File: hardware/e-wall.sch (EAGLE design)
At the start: 20 parts, among them IC1 74HCT595N, IC2 74HCT595N, IC3 74HCT595N, IC4 ULN2803, IC5 ULN2803, IC6 ULN2803, T1 BC547, T2 BC557, T3 BC547

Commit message: Spannungsteiler für SOMI
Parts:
- added R8: 20k, resistor:R-EU_0309/10
- added R9: 30k, resistor:R-EU_0309/10
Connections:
- new net N$28: R8.1, R9.2, U$1.14
- net GND: now also R9.1
- net SOMI: now also R8.2; no longer U$1.14
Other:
- note added: "Treiber"
- note removed: "Treiber für LED"
- note removed: "Treiber für Lüfter"
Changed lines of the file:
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@@
 <grid distance="0.1" unitdist="inch" unit="inch" style="lines" multiple="1" display="no" altdistance="0.01" altunitdist="inch" altunit="inch"/>
 <layers>
-<layer number="1" name="Top" color="4" fill="1" visible="yes" active="no"/>
-<layer number="16" name="Bottom" color="1" fill="1" visible="yes" active="no"/>
-<layer number="17" name="Pads" color="2" fill="1" visible="yes" active="no"/>
-<layer number="18" name="Vias" color="2" fill="1" visible="yes" active="no"/>
-<layer number="19" name="Unrouted" color="6" fill="1" visible="yes" active="no"/>
-<layer number="20" name="Dimension" color="15" fill="1" visible="yes" active="no"/>
-<layer number="21" name="tPlace" color="7" fill="1" visible="yes" active="no"/>
-<layer number="22" name="bPlace" color="7" fill="1" visible="yes" active="no"/>
-<layer number="23" name="tOrigins" color="15" fill="1" visible="yes" active="no"/>
-<layer number="24" name="bOrigins" color="15" fill="1" visible="yes" active="no"/>
-<layer number="25" name="tNames" color="7" fill="1" visible="yes" active="no"/>
-<layer number="26" name="bNames" color="7" fill="1" visible="yes" active="no"/>
-<layer number="27" name="tValues" color="7" fill="1" visible="yes" active="no"/>
-<layer number="28" name="bValues" color="7" fill="1" visible="yes" active="no"/>
+<layer number="1" name="Top" color="4" fill="1" visible="no" active="no"/>
+<layer number="16" name="Bottom" color="1" fill="1" visible="no" active="no"/>
+<layer number="17" name="Pads" color="2" fill="1" visible="no" active="no"/>
+<layer number="18" name="Vias" color="2" fill="1" visible="no" active="no"/>
+<layer number="19" name="Unrouted" color="6" fill="1" visible="no" active="no"/>
+<layer number="20" name="Dimension" color="15" fill="1" visible="no" active="no"/>
+<layer number="21" name="tPlace" color="7" fill="1" visible="no" active="no"/>
+<layer number="22" name="bPlace" color="7" fill="1" visible="no" active="no"/>
+<layer number="23" name="tOrigins" color="15" fill="1" visible="no" active="no"/>
+<layer number="24" name="bOrigins" color="15" fill="1" visible="no" active="no"/>
+<layer number="25" name="tNames" color="7" fill="1" visible="no" active="no"/>
+<layer number="26" name="bNames" color="7" fill="1" visible="no" active="no"/>
+<layer number="27" name="tValues" color="7" fill="1" visible="no" active="no"/>
+<layer number="28" name="bValues" color="7" fill="1" visible="no" active="no"/>
 <layer number="29" name="tStop" color="7" fill="3" visible="no" active="no"/>
 <layer number="30" name="bStop" color="7" fill="6" visible="no" active="no"/>
@@
 <layer number="35" name="tGlue" color="7" fill="4" visible="no" active="no"/>
 <layer number="36" name="bGlue" color="7" fill="5" visible="no" active="no"/>
-<layer number="37" name="tTest" color="7" fill="1" visible="yes" active="no"/>
-<layer number="38" name="bTest" color="7" fill="1" visible="yes" active="no"/>
+<layer number="37" name="tTest" color="7" fill="1" visible="no" active="no"/>
+<layer number="38" name="bTest" color="7" fill="1" visible="no" active="no"/>
 <layer number="39" name="tKeepout" color="4" fill="11" visible="no" active="no"/>
 <layer number="40" name="bKeepout" color="1" fill="11" visible="no" active="no"/>
@@
 <layer number="44" name="Drills" color="7" fill="1" visible="no" active="no"/>
 <layer number="45" name="Holes" color="7" fill="1" visible="no" active="no"/>
-<layer number="46" name="Milling" color="3" fill="1" visible="yes" active="no"/>
-<layer number="47" name="Measures" color="7" fill="1" visible="yes" active="no"/>
-<layer number="48" name="Document" color="7" fill="1" visible="yes" active="no"/>
-<layer number="49" name="Reference" color="7" fill="1" visible="yes" active="no"/>
-<layer number="51" name="tDocu" color="7" fill="1" visible="yes" active="no"/>
-<layer number="52" name="bDocu" color="7" fill="1" visible="yes" active="no"/>
+<layer number="46" name="Milling" color="3" fill="1" visible="no" active="no"/>
+<layer number="47" name="Measures" color="7" fill="1" visible="no" active="no"/>
+<layer number="48" name="Document" color="7" fill="1" visible="no" active="no"/>
+<layer number="49" name="Reference" color="7" fill="1" visible="no" active="no"/>
+<layer number="51" name="tDocu" color="7" fill="1" visible="no" active="no"/>
+<layer number="52" name="bDocu" color="7" fill="1" visible="no" active="no"/>
 <layer number="91" name="Nets" color="2" fill="1" visible="yes" active="yes"/>
 <layer number="92" name="Busses" color="1" fill="1" visible="yes" active="yes"/>
@@
 <part name="P+4" library="supply1" deviceset="VCC" device=""/>
 <part name="P+5" library="supply1" deviceset="VCC" device=""/>
+<part name="R8" library="resistor" deviceset="R-EU_" device="0309/10" value="20k"/>
+<part name="R9" library="resistor" deviceset="R-EU_" device="0309/10" value="30k"/>
+<part name="GND9" library="supply1" deviceset="GND" device=""/>
 </parts>
 <sheets>
@@
 <plain>
 <wire x1="180.34" y1="0" x2="185.42" y2="-5.08" width="0.1524" layer="97" curve="90"/>
-<wire x1="185.42" y1="-5.08" x2="246.38" y2="-5.08" width="0.1524" layer="97"/>
-<wire x1="246.38" y1="-5.08" x2="251.46" y2="-10.16" width="0.1524" layer="97" curve="-90"/>
-<wire x1="251.46" y1="-10.16" x2="256.54" y2="-5.08" width="0.1524" layer="97" curve="-90"/>
-<wire x1="256.54" y1="-5.08" x2="317.5" y2="-5.08" width="0.1524" layer="97"/>
-<wire x1="317.5" y1="-5.08" x2="322.58" y2="0" width="0.1524" layer="97" curve="90"/>
-<wire x1="325.12" y1="0" x2="330.2" y2="-5.08" width="0.1524" layer="97" curve="90"/>
-<wire x1="330.2" y1="-5.08" x2="391.16" y2="-5.08" width="0.1524" layer="97"/>
-<wire x1="391.16" y1="-5.08" x2="396.24" y2="-10.16" width="0.1524" layer="97" curve="-90"/>
-<wire x1="396.24" y1="-10.16" x2="401.32" y2="-5.08" width="0.1524" layer="97" curve="-90"/>
-<wire x1="401.32" y1="-5.08" x2="462.28" y2="-5.08" width="0.1524" layer="97"/>
-<wire x1="462.28" y1="-5.08" x2="467.36" y2="0" width="0.1524" layer="97" curve="90"/>
-<text x="243.84" y="-15.24" size="1.778" layer="97">Treiber für LED</text>
-<text x="388.62" y="-15.24" size="1.778" layer="97">Treiber für Lüfter</text>
+<wire x1="185.42" y1="-5.08" x2="198.12" y2="-5.08" width="0.1524" layer="97"/>
+<wire x1="198.12" y1="-5.08" x2="203.2" y2="-10.16" width="0.1524" layer="97" curve="-90"/>
+<wire x1="203.2" y1="-10.16" x2="208.28" y2="-5.08" width="0.1524" layer="97" curve="-90"/>
+<wire x1="208.28" y1="-5.08" x2="226.06" y2="-5.08" width="0.1524" layer="97"/>
+<wire x1="226.06" y1="-5.08" x2="231.14" y2="0" width="0.1524" layer="97" curve="90"/>
+<text x="195.58" y="-15.24" size="1.778" layer="97">Treiber</text>
 <wire x1="165.1" y1="0" x2="160.02" y2="-5.08" width="0.1524" layer="97" curve="-90"/>
 <wire x1="160.02" y1="-5.08" x2="142.24" y2="-5.08" width="0.1524" layer="97"/>
@@
 <instance part="P+4" gate="VCC" x="66.04" y="78.74"/>
 <instance part="P+5" gate="VCC" x="99.06" y="50.8"/>
+<instance part="R8" gate="G$1" x="104.14" y="30.48" rot="R90"/>
+<instance part="R9" gate="G$1" x="104.14" y="15.24" rot="R90"/>
+<instance part="GND9" gate="1" x="104.14" y="5.08"/>
 </instances>
 <busses>
@@
 <wire x1="88.9" y1="43.18" x2="96.52" y2="43.18" width="0.1524" layer="91"/>
 <junction x="96.52" y="43.18"/>
+</segment>
+<segment>
+<pinref part="GND9" gate="1" pin="GND"/>
+<pinref part="R9" gate="G$1" pin="1"/>
+<wire x1="104.14" y1="7.62" x2="104.14" y2="10.16" width="0.1524" layer="91"/>
 </segment>
 </net>
@@
 <wire x1="154.94" y1="12.7" x2="154.94" y2="5.08" width="0.1524" layer="91"/>
 <wire x1="154.94" y1="5.08" x2="109.22" y2="5.08" width="0.1524" layer="91"/>
-<wire x1="109.22" y1="5.08" x2="109.22" y2="58.42" width="0.1524" layer="91"/>
-<pinref part="U$1" gate="G$1" pin="14"/>
-<wire x1="109.22" y1="58.42" x2="88.9" y2="58.42" width="0.1524" layer="91"/>
-<label x="91.44" y="58.42" size="1.778" layer="95"/>
+<wire x1="109.22" y1="5.08" x2="109.22" y2="35.56" width="0.1524" layer="91"/>
+<pinref part="R8" gate="G$1" pin="2"/>
+<wire x1="104.14" y1="35.56" x2="109.22" y2="35.56" width="0.1524" layer="91"/>
 </segment>
 </net>
@@
 </segment>
 </net>
+<net name="N$28" class="0">
+<segment>
+<pinref part="U$1" gate="G$1" pin="14"/>
+<wire x1="101.6" y1="58.42" x2="88.9" y2="58.42" width="0.1524" layer="91"/>
+<pinref part="R8" gate="G$1" pin="1"/>
+<pinref part="R9" gate="G$1" pin="2"/>
+<wire x1="104.14" y1="20.32" x2="104.14" y2="22.86" width="0.1524" layer="91"/>
+<wire x1="104.14" y1="22.86" x2="104.14" y2="25.4" width="0.1524" layer="91"/>
+<junction x="104.14" y="22.86"/>
+<wire x1="104.14" y1="22.86" x2="101.6" y2="22.86" width="0.1524" layer="91"/>
+<wire x1="101.6" y1="22.86" x2="101.6" y2="58.42" width="0.1524" layer="91"/>
+<label x="91.44" y="58.42" size="1.778" layer="95"/>
+</segment>
+</net>

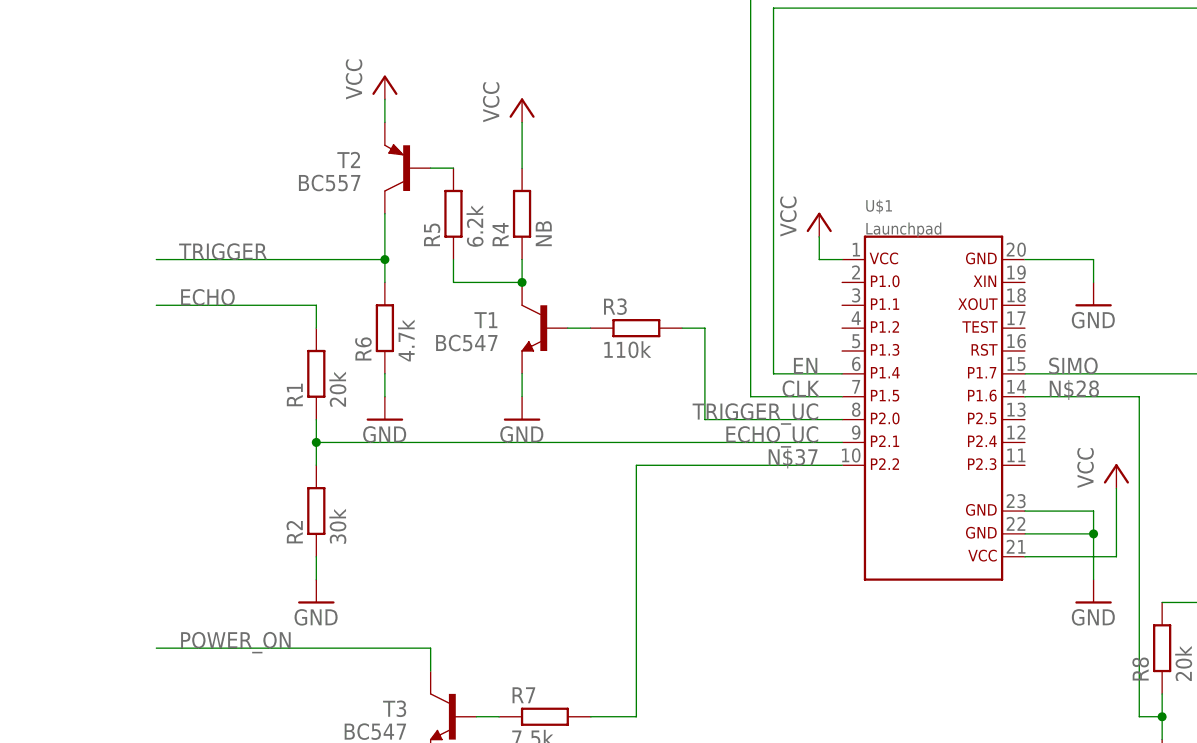
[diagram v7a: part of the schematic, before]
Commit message: Ultraschallsensor eingebaut
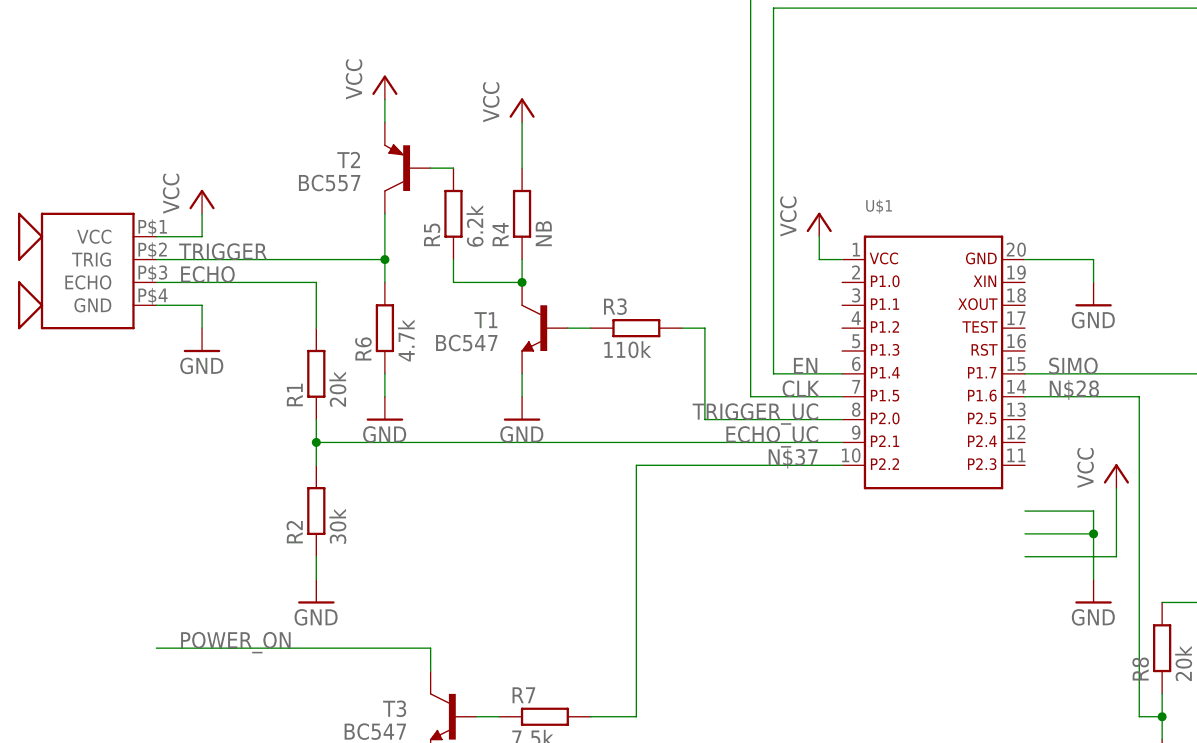
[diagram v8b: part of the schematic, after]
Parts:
- added U$2: (no value), ultrasonic:HC-SR04
- R5: device resistor:R-EU_0309/10 -> resistor:R-EU_0309/V
- U$1: value Launchpad -> (none); device msp430launchpad:MSP430LAUNCHPAD_FULL -> msp430launchpad:MSP430LAUNCHPAD_BASIC
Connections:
- net ECHO: now also U$2.ECHO
- net GND: now also U$2.GND; no longer U$1.22, U$1.23
- net TRIGGER: now also U$2.TRIG
- net VCC: now also U$2.VCC; no longer U$1.21
